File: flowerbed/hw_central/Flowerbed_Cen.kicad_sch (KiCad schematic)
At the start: 17 parts, among them J1 USB_C_Receptacle_PowerOnly_6P, J2 Conn_01x04, J3 Conn_01x08, J4 Conn_01x04, U1 AMS1117-3.3, U2 STM32G030F6Px

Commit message: Finish flowerbed central schematic
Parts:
- removed C3: 22u, Capacitor_SMD:CP_Elec_5x5.4, symbol Device:C_Polarized
- removed U1: AMS1117-3.3, Package_TO_SOT_SMD:SOT-223-3_TabPin2, symbol Regulator_Linear:AMS1117-3.3
- added C3: 22p, Capacitor_SMD:C_0603_1608Metric, symbol Device:C
- added C4, C5: 22u, Capacitor_SMD:C_0603_1608Metric, symbol Device:C
- added C8: 100n, Capacitor_SMD:C_0603_1608Metric, symbol Device:C
- added L1: 4.7u, Inductor_SMD:L_Sunlord_MWSA1004S, symbol Device:L
- added R3: 100k, Resistor_SMD:R_0603_1608Metric, symbol Device:R
- added R4: 22k, Resistor_SMD:R_0603_1608Metric, symbol Device:R
- added R7, R8: 3.3k, Resistor_SMD:R_0603_1608Metric, symbol Device:R
- added U1: MT2492, Package_TO_SOT_SMD:SOT-23-6, symbol Flowerbed_Cen_symbols:MT2492
- added U3: LTC4311CSC6#TRPBF, Flowerbed_Cen_footprints:SOT65P210X100-6N, symbol Flowerbed_Cen_symbols:LTC4311CSC6#TRPBF
- C1: value 10u -> 22u
- C2: value 22u -> 22n; footprint Capacitor_SMD:C_0805_2012Metric -> Capacitor_SMD:C_0603_1608Metric
- J1: footprint FUNgi_footprints:USB_C_Receptacle -> Flowerbed_Cen_footprints:USB_C_Receptacle
- renumbered C4 to C6, C5 to C7
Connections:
- net GND: now also C4.2, C5.2, C8.2, R4.2, U1.2 (GND), U3.2 (GND_1), U3.5 (GND_2); no longer C2.2
- net I2C2_SCL: now also R7.2, U3.6 (BUS1)
- net I2C2_SDA: now also R8.2, U3.4 (BUS2)
- net VBUS: now also U1.4 (EN), U1.5 (IN)
- net VDD: now also C3.1, C4.1, C5.1, C8.1, L1.2, R3.1, R7.1, R8.1, U3.1 (VCC), U3.3 (ENABLE); no longer C2.1
- new net: C2.1, U1.1 (BS)
- new net: C3.2, R3.2, R4.1, U1.3 (FB)
- new net: C2.2, L1.1, U1.6 (SW)
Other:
- note added: "FB ref. 0.6 V typ."
- note added: "Set output = 3.32 V"
- moved on the sheet: J4

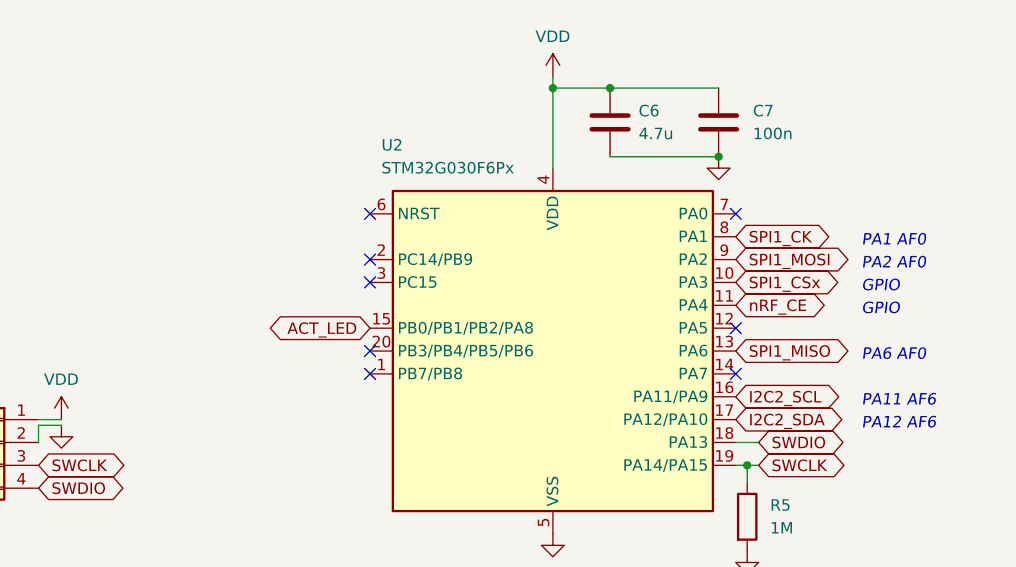
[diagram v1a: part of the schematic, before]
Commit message: Finish flowerbed central board; submit for fab
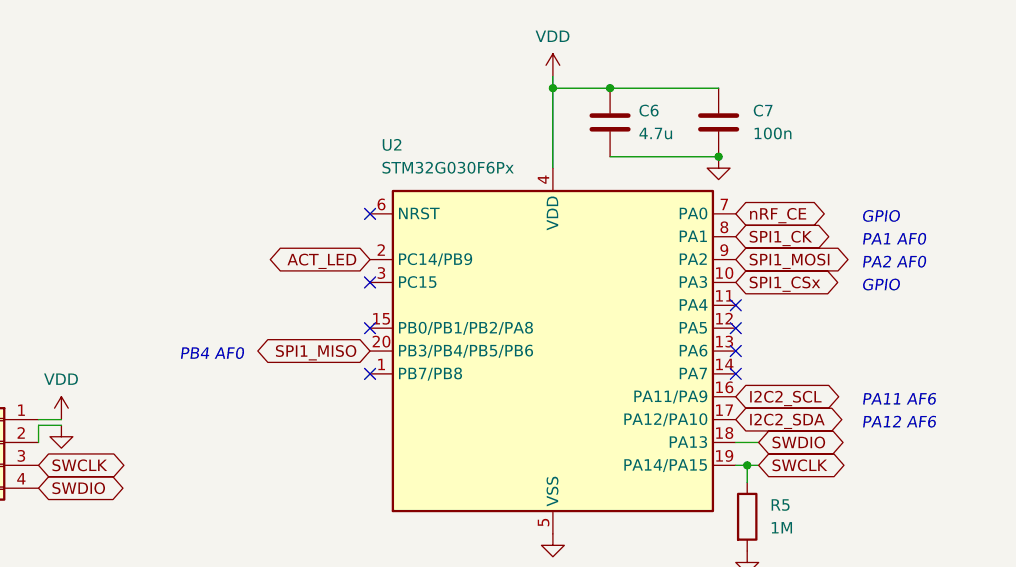
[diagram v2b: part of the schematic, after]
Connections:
- net ACT_LED: now also U2.2 (PC14/PB9); no longer U2.15 (PB0/PB1/PB2/PA8)
- net SPI1_MISO: now also U2.20 (PB3/PB4/PB5/PB6); no longer U2.13 (PA6)
- net nRF_CE: now also U2.7 (PA0); no longer U2.11 (PA4)
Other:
- note added: "PB4 AF0"
- note removed: "PA6 AF0"
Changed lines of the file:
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@@
   (no_connect (at 24.765 51.435))
   (no_connect (at 85.725 90.805))
-  (no_connect (at 126.365 90.805))
-  (no_connect (at 85.725 106.045))
+  (no_connect (at 126.365 106.045))
+  (no_connect (at 85.725 103.505))
   (no_connect (at 48.895 151.765))
   (no_connect (at 85.725 98.425))
@@
   (no_connect (at 85.725 108.585))
   (no_connect (at 126.365 108.585))
-  (no_connect (at 85.725 95.885))
+  (no_connect (at 126.365 100.965))
   (wire (pts (xy 50.8 168.91) (xy 54.61 168.91))
     (stroke (width 0) (type default))
@@
     (effects (font (size 1.27 1.27) italic) (justify left bottom))
   )
-  (text "GPIO" (at 140.335 102.235 0)
+  (text "GPIO" (at 140.335 92.075 0)
     (effects (font (size 1.27 1.27) italic) (justify left bottom))
   )
@@
     (effects (font (size 1.27 1.27) italic) (justify left bottom))
   )
-  (text "PA6 AF0" (at 140.335 107.315 0)
-    (effects (font (size 1.27 1.27) italic) (justify left bottom))
+  (text "PB4 AF0" (at 71.755 107.315 0)
+    (effects (font (size 1.27 1.27) italic) (justify right bottom))
   )
   (text "FB ref.\n0.6 V typ." (at 107.315 45.085 0)
@@
     )
   )
-  (global_label "nRF_CE" (shape bidirectional) (at 126.365 100.965 0) (fields_autoplaced)
-    (effects (font (size 1.27 1.27)) (justify left))
-    (property "Intersheetrefs" "${INTERSHEET_REFS}" (at 137.3557 100.965 0)
-      (effects (font (size 1.27 1.27)) (justify left) hide)
-    )
-  )
-  (global_label "SPI1_MISO" (shape bidirectional) (at 126.365 106.045 0) (fields_autoplaced)
-    (effects (font (size 1.27 1.27)) (justify left))
-    (property "Intersheetrefs" "${INTERSHEET_REFS}" (at 140.3191 106.045 0)
-      (effects (font (size 1.27 1.27)) (justify left) hide)
+  (global_label "nRF_CE" (shape bidirectional) (at 126.365 90.805 0) (fields_autoplaced)
+    (effects (font (size 1.27 1.27)) (justify left))
+    (property "Intersheetrefs" "${INTERSHEET_REFS}" (at 137.3557 90.805 0)
+      (effects (font (size 1.27 1.27)) (justify left) hide)
+    )
+  )
+  (global_label "SPI1_MISO" (shape bidirectional) (at 85.725 106.045 180) (fields_autoplaced)
+    (effects (font (size 1.27 1.27)) (justify right))
+    (property "Intersheetrefs" "${INTERSHEET_REFS}" (at 71.7709 106.045 0)
+      (effects (font (size 1.27 1.27)) (justify right) hide)
     )
   )
@@
     )
   )
-  (global_label "ACT_LED" (shape bidirectional) (at 85.725 103.505 180) (fields_autoplaced)
+  (global_label "ACT_LED" (shape bidirectional) (at 85.725 95.885 180) (fields_autoplaced)
     (effects (font (size 1.27 1.27)) (justify right))
-    (property "Intersheetrefs" "${INTERSHEET_REFS}" (at 73.8876 103.505 0)
+    (property "Intersheetrefs" "${INTERSHEET_REFS}" (at 73.8876 95.885 0)
       (effects (font (size 1.27 1.27)) (justify right) hide)
     )
